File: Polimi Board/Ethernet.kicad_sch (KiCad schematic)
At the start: 17 parts, among them J6 RJ45_Wuerth_7499010121A, U3 LAN8742A

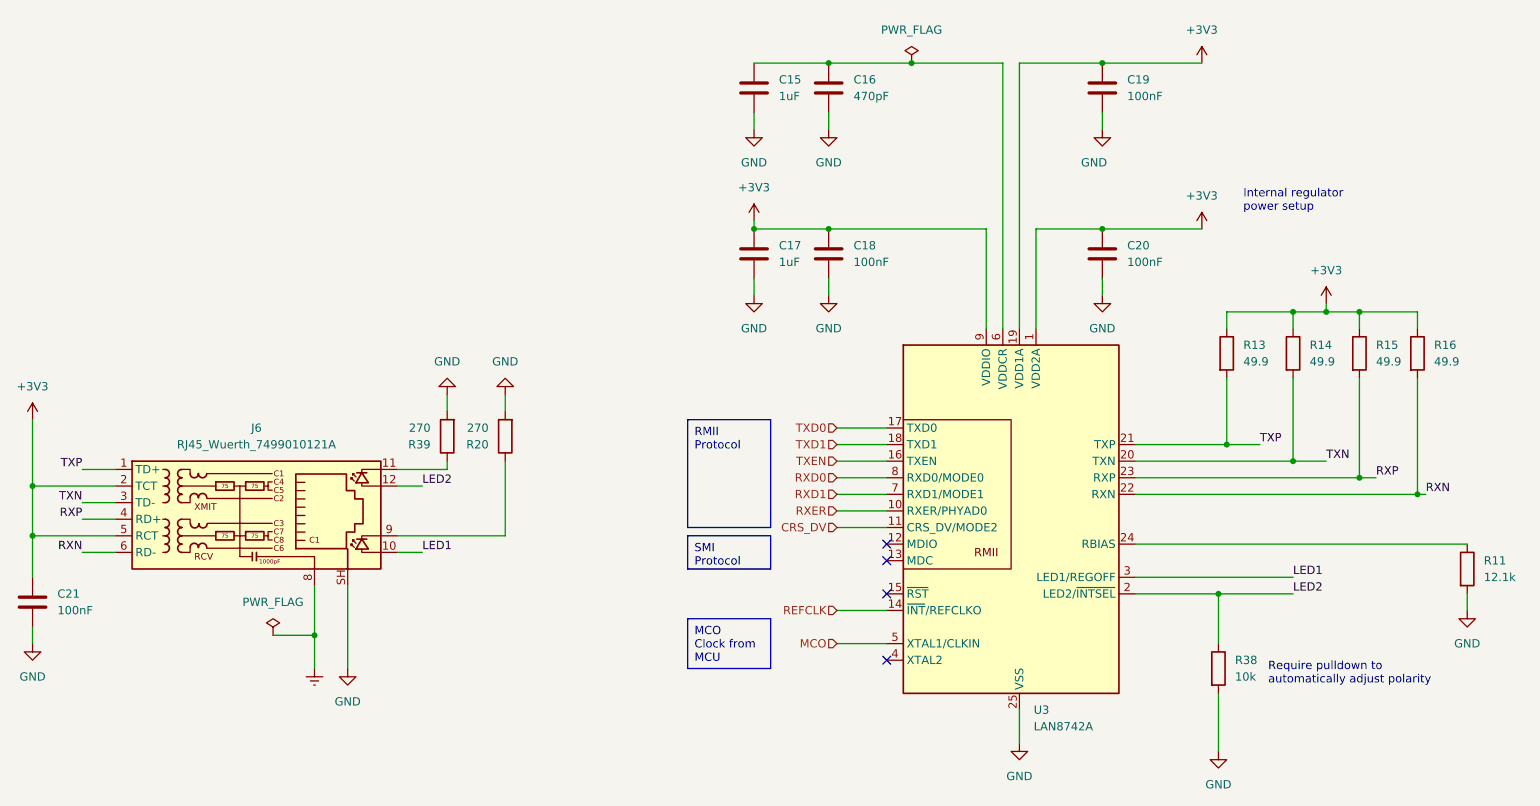
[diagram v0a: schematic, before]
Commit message: Added footprint from Mouser
readu for wiring
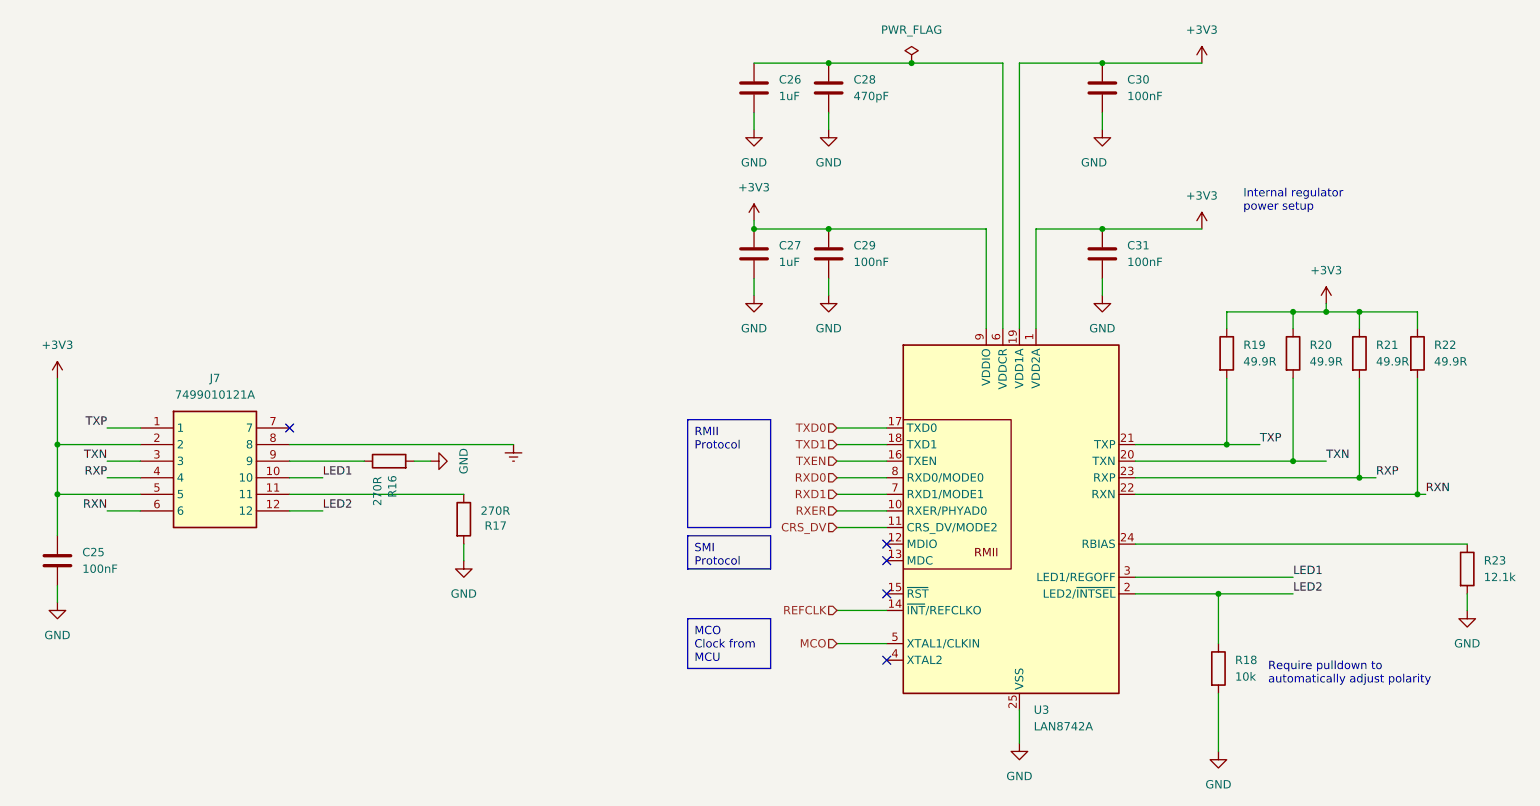
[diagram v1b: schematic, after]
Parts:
- removed C21: 100nF, symbol Device:C
- removed J6: RJ45_Wuerth_7499010121A, Connector_RJ:RJ45_Wuerth_7499010121A_Horizontal, symbol Connector:RJ45_Wuerth_7499010121A
- removed R20, R39: 270, symbol Device:R
- added C25: 100nF, Capacitor_SMD:C_0603_1608Metric_Pad1.08x0.95mm_HandSolder, symbol Device:C
- added J7: 7499010121A, SamacSys_Parts:WURTH-7499010121A, symbol SamacSys_Parts:7499010121A
- added R16, R17: 270R, Resistor_SMD:R_0603_1608Metric_Pad0.98x0.95mm_HandSolder, symbol Device:R
- C26: renamed from C15; footprint (none) -> Capacitor_SMD:C_0603_1608Metric_Pad1.08x0.95mm_HandSolder
- C27: renamed from C17; footprint (none) -> Capacitor_SMD:C_0603_1608Metric_Pad1.08x0.95mm_HandSolder
- C28: renamed from C16; footprint (none) -> Capacitor_SMD:C_0603_1608Metric_Pad1.08x0.95mm_HandSolder
- C29: renamed from C18; footprint (none) -> Capacitor_SMD:C_0603_1608Metric_Pad1.08x0.95mm_HandSolder
- C30: renamed from C19; footprint (none) -> Capacitor_SMD:C_0603_1608Metric_Pad1.08x0.95mm_HandSolder
- C31: renamed from C20; footprint (none) -> Capacitor_SMD:C_0603_1608Metric_Pad1.08x0.95mm_HandSolder
- R18: renamed from R38; footprint (none) -> Resistor_SMD:R_0603_1608Metric_Pad0.98x0.95mm_HandSolder
- R19: renamed from R13; value 49.9 -> 49.9R; footprint (none) -> Resistor_SMD:R_0603_1608Metric_Pad0.98x0.95mm_HandSolder
- R20: renamed from R14; value 49.9 -> 49.9R; footprint (none) -> Resistor_SMD:R_0603_1608Metric_Pad0.98x0.95mm_HandSolder
- R21: renamed from R15; value 49.9 -> 49.9R; footprint (none) -> Resistor_SMD:R_0603_1608Metric_Pad0.98x0.95mm_HandSolder
- R22: renamed from R16; value 49.9 -> 49.9R; footprint (none) -> Resistor_SMD:R_0603_1608Metric_Pad0.98x0.95mm_HandSolder
- R23: renamed from R11; footprint (none) -> Resistor_SMD:R_0603_1608Metric_Pad0.98x0.95mm_HandSolder
- U3: footprint Package_DFN_QFN:VQFN-24-1EP_4x4mm_P0.5mm_EP2.5x2.5mm_ThermalVias -> SamacSys_Parts:QFN50P400X400X100-25N-D
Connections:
- net +3V3: now also C25.1, J7.2, J7.5
- net Earth: now also J7.8
- net GND: now also C25.2, R16.2, R17.2
- net LED1: now also J7.10
- net LED2: now also J7.12
- net RXN: now also J7.6
- net RXP: now also J7.4
- net TXN: now also J7.3
- net TXP: now also J7.1
- new net: J7.9, R16.1
- new net: J7.11, R17.1
- no-connect marks 4 -> 5

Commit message: PCB wip
before holidays
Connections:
- net GND: now also J7.11, J7.9; no longer R16.2, R17.2
- net LED1: now also R16.2; no longer J7.10
- net LED2: now also R17.1; no longer J7.12
- net at R16.1: now also J7.10; no longer J7.9
- new net: J7.12, R17.2
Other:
- moved on the sheet: R16, R17
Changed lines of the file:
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@@
+	(wire
+		(pts
+			(xy 88.9 102.87) (xy 91.44 102.87)
+		)
+		(stroke
+			(width 0)
+			(type default)
+		)
+	)
 	(wire
 		(pts
@@
 	(wire
 		(pts
-			(xy 77.47 102.87) (xy 82.55 102.87)
+			(xy 77.47 102.87) (xy 81.28 102.87)
 		)
 		(stroke
@@
 	(wire
 		(pts
-			(xy 77.47 100.33) (xy 104.14 100.33)
+			(xy 77.47 100.33) (xy 99.06 100.33)
 		)
 		(stroke
@@
 	(wire
 		(pts
-			(xy 96.52 95.25) (xy 99.06 95.25)
-		)
-		(stroke
-			(width 0)
-			(type default)
-		)
-	)
-	(wire
-		(pts
 			(xy 148.59 34.29) (xy 160.02 34.29)
 		)
@@
 	(wire
 		(pts
-			(xy 82.55 97.79) (xy 77.47 97.79)
+			(xy 81.28 97.79) (xy 77.47 97.79)
 		)
 		(stroke
@@
 	(wire
 		(pts
-			(xy 104.14 107.95) (xy 104.14 110.49)
-		)
-		(stroke
-			(width 0)
-			(type default)
-		)
-	)
-	(wire
-		(pts
 			(xy 49.53 95.25) (xy 54.61 95.25)
 		)
@@
 	(wire
 		(pts
+			(xy 91.44 97.79) (xy 88.9 97.79)
+		)
+		(stroke
+			(width 0)
+			(type default)
+		)
+	)
+	(wire
+		(pts
 			(xy 207.01 92.71) (xy 220.98 92.71)
 		)
@@
 	(wire
 		(pts
-			(xy 77.47 95.25) (xy 88.9 95.25)
+			(xy 77.47 95.25) (xy 99.06 95.25)
 		)
 		(stroke
@@
 	)
 	(label "LED2"
-		(at 82.55 102.87 0)
+		(at 91.44 102.87 0)
 		(fields_autoplaced yes)
 		(effects
@@
 	)
 	(label "LED1"
-		(at 82.55 97.79 0)
+		(at 91.44 97.79 0)
 		(fields_autoplaced yes)
 		(effects
@@
 	(symbol
 		(lib_id "Device:R")
-		(at 92.71 95.25 90)
+		(at 85.09 97.79 90)
 		(unit 1)
 		(exclude_from_sim no)
@@
 		(dnp no)
 		(property "Reference" "R16"
-			(at 93.218 100.838 0)
+			(at 85.598 103.378 0)
 			(effects
 				(font
@@
 		)
 		(property "Value" "270R"
-			(at 90.932 102.108 0)
+			(at 83.312 104.648 0)
 			(effects
 				(font
@@
 		)
 		(property "Footprint" "Resistor_SMD:R_0603_1608Metric_Pad0.98x0.95mm_HandSolder"
-			(at 92.71 97.028 90)
+			(at 85.09 99.568 90)
 			(effects
 				(font
@@
 		)
 		(property "Datasheet" "~"
-			(at 92.71 95.25 0)
+			(at 85.09 97.79 0)
 			(effects
 				(font
@@
 		)
 		(property "Description" ""
-			(at 92.71 95.25 0)
+			(at 85.09 97.79 0)
 			(effects
 				(font
@@
 	(symbol
 		(lib_id "Device:R")
-		(at 104.14 104.14 0)
+		(at 85.09 102.87 270)
 		(unit 1)
 		(exclude_from_sim no)
@@
 		(dnp no)
 		(property "Reference" "R17"
-			(at 110.744 105.156 0)
+			(at 84.074 109.474 0)
 			(effects
 				(font
@@
 		)
 		(property "Value" "270R"
-			(at 111.252 102.87 0)
+			(at 86.36 109.982 0)
 			(effects
 				(font
@@
 		)
 		(property "Footprint" "Resistor_SMD:R_0603_1608Metric_Pad0.98x0.95mm_HandSolder"
-			(at 102.362 104.14 90)
+			(at 85.09 101.092 90)
 			(effects
 				(font
@@
 		)
 		(property "Datasheet" "~"
-			(at 104.14 104.14 0)
+			(at 85.09 102.87 0)
 			(effects
 				(font
@@
 		)
 		(property "Description" ""
-			(at 104.14 104.14 0)
+			(at 85.09 102.87 0)
 			(effects
 				(font
@@
 	(symbol
 		(lib_id "power:GND")
-		(at 104.14 110.49 0)
+		(at 99.06 100.33 90)
 		(unit 1)
 		(exclude_from_sim no)
@@
 		(fields_autoplaced yes)
 		(property "Reference" "#PWR054"
-			(at 104.14 116.84 0)
+			(at 105.41 100.33 0)
 			(effects
 				(font
@@
 		)
 		(property "Value" "GND"
-			(at 104.14 115.57 0)
-			(effects
-				(font
-					(size 1.27 1.27)
-				)
+			(at 102.87 100.3299 90)
+			(effects
+				(font
+					(size 1.27 1.27)
+				)
+				(justify right)
 			)
 		)
 		(property "Footprint" ""
-			(at 104.14 110.49 0)
+			(at 99.06 100.33 0)
 			(effects
 				(font
@@
 		)
 		(property "Datasheet" ""
-			(at 104.14 110.49 0)
+			(at 99.06 100.33 0)
 			(effects
 				(font
@@
 		)
 		(property "Description" ""
-			(at 104.14 110.49 0)
-			(effects
-				(font
+			(at 99.06 100.33 0)
+			(effects
+				(font

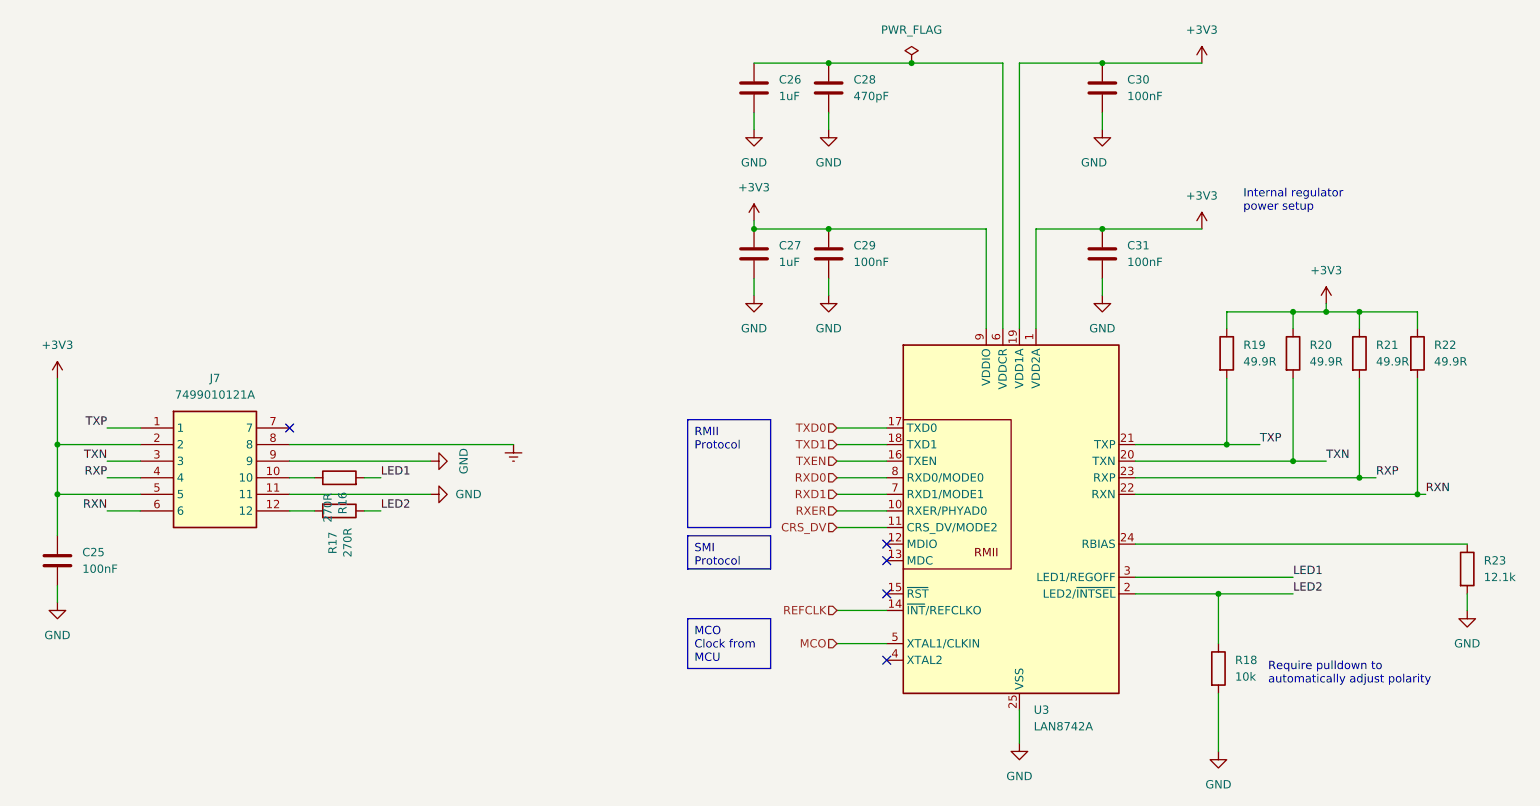
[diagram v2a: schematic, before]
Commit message: Solved issues
3.3V 3V3 and others
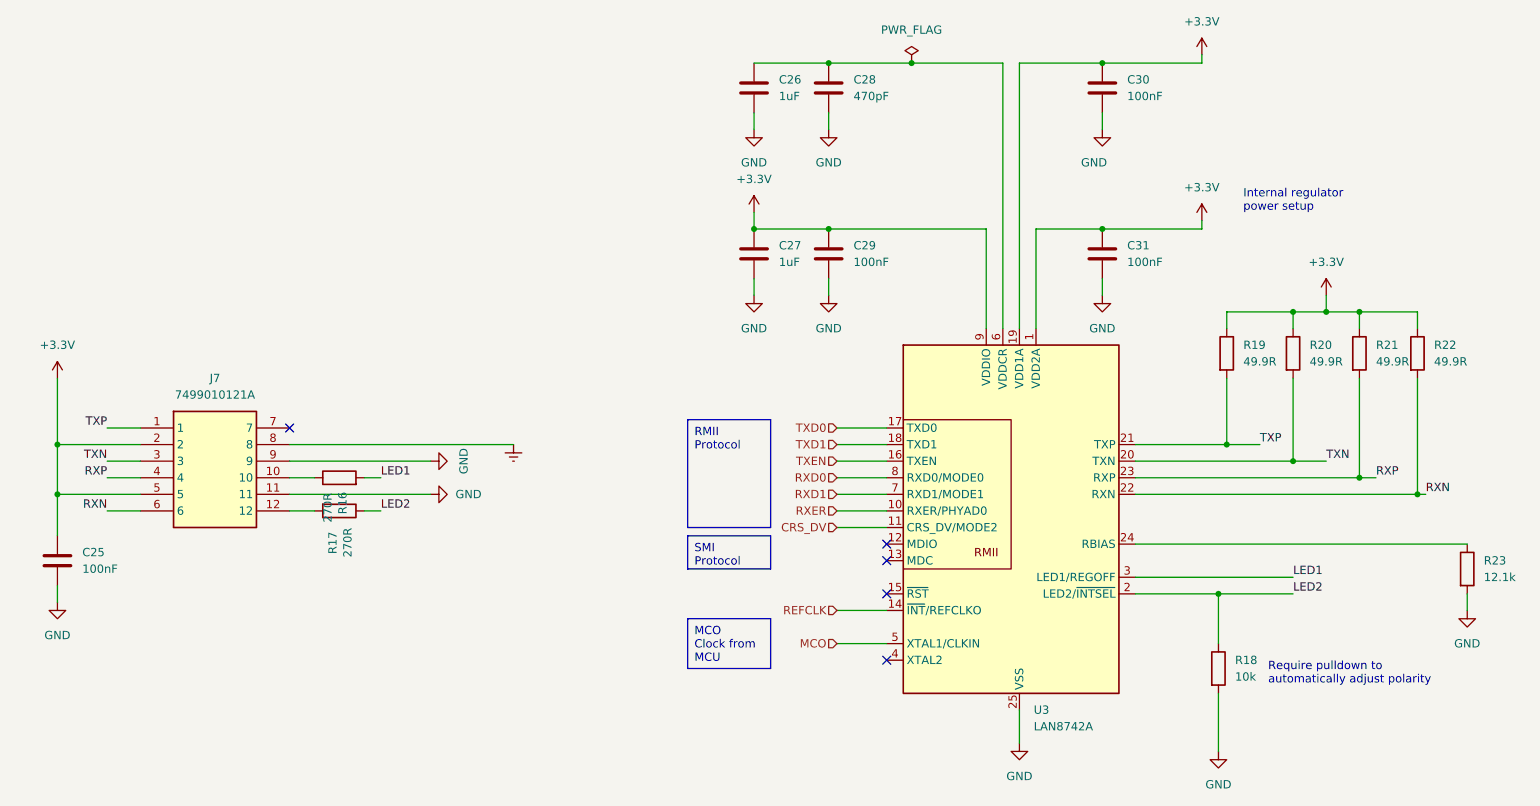
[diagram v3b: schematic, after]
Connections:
- net +3V3 renamed +3.3V
